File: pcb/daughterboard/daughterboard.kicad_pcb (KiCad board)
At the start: 2 copper layers, 20 x 20 mm, 11 parts, among them J1 Conn_01x04

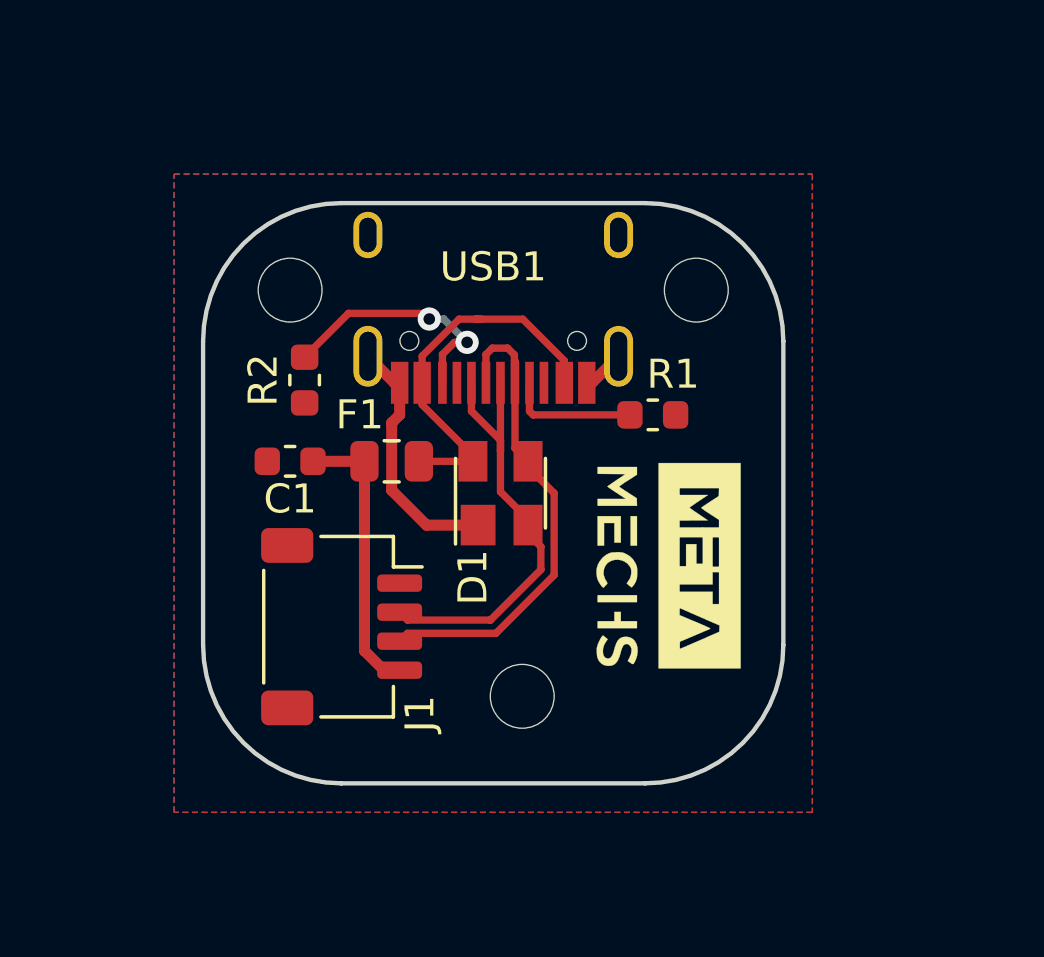
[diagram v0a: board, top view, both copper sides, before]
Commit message: redid daughterboard
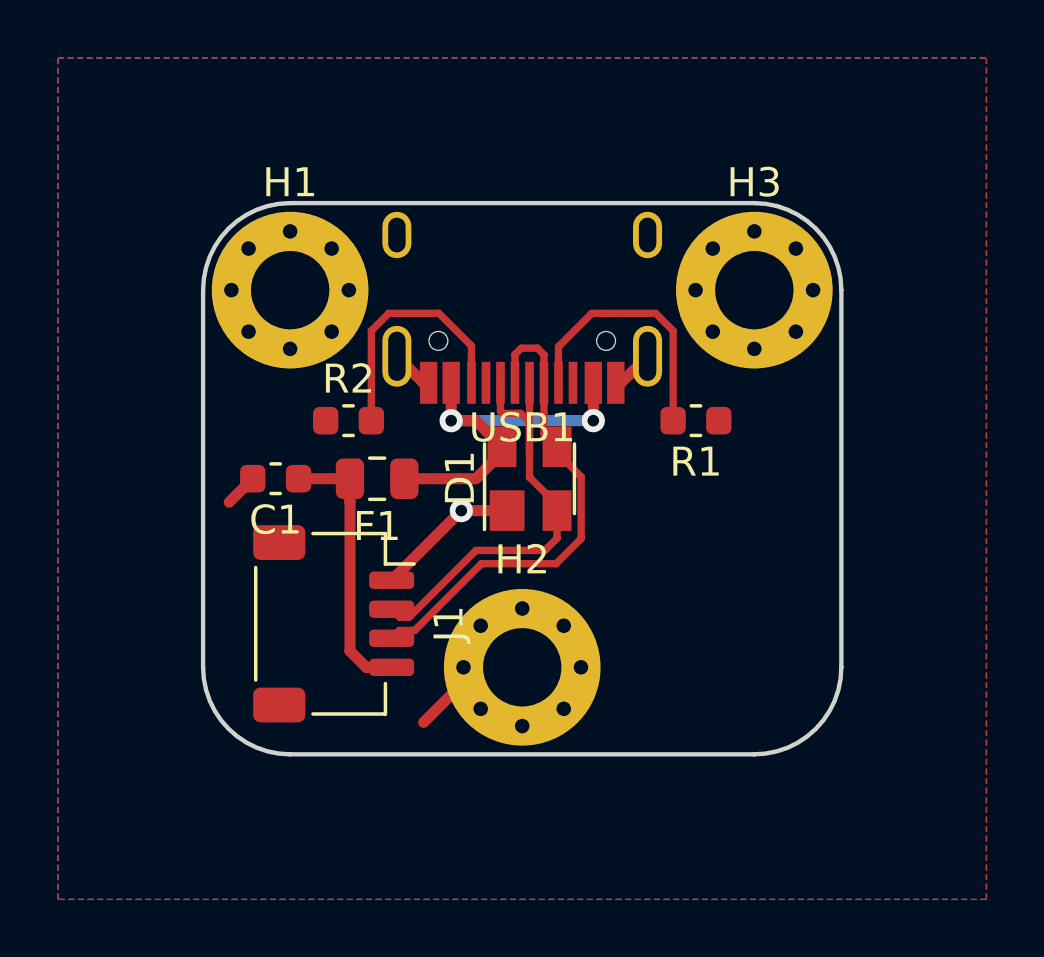
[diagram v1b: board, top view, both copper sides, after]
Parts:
- removed G***: LOGO, logo:logo tiny vert
- removed REF** (x3): MountingHole_2.2mm_M2, keebs:MountingHole_2.2mm_M2
- added H1: MountingHole_Pad, keebs:m2.5_pad_via, F.Cu at (3.00, 3.00)
- added H2: MountingHole_Pad, keebs:m2.5_pad_via, F.Cu at (11.0, 16.0)
- added H3: MountingHole_Pad, keebs:m2.5_pad_via, F.Cu at (19.0, 3.00)
- moved R2 2.06 mm to (5.01, 7.50), turned to 0 degrees
- moved R1 1.50 mm to (17.0, 7.50)
- moved D1 1.12 mm to (11.2, 9.50)
- moved USB1 1.00 mm to (11.0, -1.50)
- moved C1 0.78 mm to (2.50, 9.50)
- moved F1 0.78 mm to (6.00, 9.50)
- moved J1 0.29 mm to (4.50, 14.5)
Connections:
- USB1 pad 3: Net-(USB1-Pad3) -> (no net)
- USB1 pad 9: Net-(USB1-Pad9) -> (no net)
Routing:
- net Net-(R1-Pad2): track 4.49 -> 9.02 mm
- net GND: track 10.2 -> 13.3 mm, vias 0 -> 1
- net /vbus: track 13.2 -> 14.1 mm, vias 0 -> 2
- net Net-(R2-Pad2): track 8.64 -> 8.54 mm, vias 2 -> 0
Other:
- board size 20 x 20 mm -> 22 x 19 mm

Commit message: gerbers
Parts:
- added G***: LOGO, logo:logo tiny vert, F.Cu at (17.8, 13.6)

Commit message: daughterboard updates
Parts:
- J1: footprint Connector_JST:JST_SH_SM04B-SRSS-TB_1x04-1MP_P1.00mm_Horizontal -> Connector_PinHeader_2.00mm:PinHeader_1x04_P2.00mm_Vertical
- moved J1 2.93 mm to (4.10, 11.6), turned to 0 degrees
- moved C1 1.10 mm to (2.50, 8.40)
- moved F1 1.10 mm to (6.00, 8.40)
- moved R2 1.01 mm to (4.40, 6.70)
- moved G*** 0.21 mm to (17.8, 13.4)
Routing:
- net GND: track 13.3 -> 4.53 mm, vias 1 -> 2
- net VCC: track 9.38 -> 12.5 mm
- net /d-: track 17.0 -> 19.6 mm
- net /d+: track 15.8 -> 18.5 mm
- net /vbus: track 14.1 -> 13.5 mm
- net Net-(R2-Pad2): track 8.54 -> 7.99 mm

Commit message: added gnd vias
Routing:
- net GND: vias 2 -> 4
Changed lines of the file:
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@@
     (thickness 1)
     (drawings 8)
-    (tracks 66)
+    (tracks 68)
     (zones 0)
     (modules 11)
@@
   (segment (start 8.9 10.6) (end 10.48 10.6) (width 0.381) (layer F.Cu) (net 2) (status 20))
   (via (at 8.9 10.6) (size 0.8) (drill 0.4) (layers F.Cu B.Cu) (net 2))
-  (via (at 1.4 11.6) (size 0.8) (drill 0.4) (layers F.Cu B.Cu) (net 2))
+  (via (at 1.2 10.6) (size 0.8) (drill 0.4) (layers F.Cu B.Cu) (net 2))
+  (via (at 1.3 16) (size 0.8) (drill 0.4) (layers F.Cu B.Cu) (net 2))
+  (via (at 1.3 13.2) (size 0.8) (drill 0.4) (layers F.Cu B.Cu) (net 2))
   (segment (start 12.2 10.4) (end 12.2 10.6) (width 0.254) (layer F.Cu) (net 3) (status 30))
   (segment (start 11.25 9.45) (end 12.2 10.4) (width 0.254) (layer F.Cu) (net 3) (status 20))
